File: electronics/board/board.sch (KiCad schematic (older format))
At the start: 55 parts, among them J1 Screw_Terminal_01x02, J10 Conn_01x02, J11 Conn_01x02, J12 Conn_01x02, J13 Conn_01x02, J14 Conn_01x02, J15 Conn_01x02, J16 Conn_01x02, J17 Conn_01x02, J18 Conn_01x02, J19 Conn_01x02, J2 Screw_Terminal_01x02, J20 Conn_01x02, J21 Conn_01x02, J22 Conn_01x02, J3 AVR-ISP-6, J4 USB_B_Micro, J5 Screw_Terminal_01x02, J6 Screw_Terminal_01x02, J7 Conn_01x02, J8 Conn_01x02, J9 Conn_01x02, Q1 IRF7404, SW1 SW_Push_Open_Dual, U1 LMV358, U2 ATmega32U4-AU, U3 LM7805_TO220, U4 ST485EBDR, U5 ULN2803A, U6 ULN2803A, Y1 Crystal 16MHz

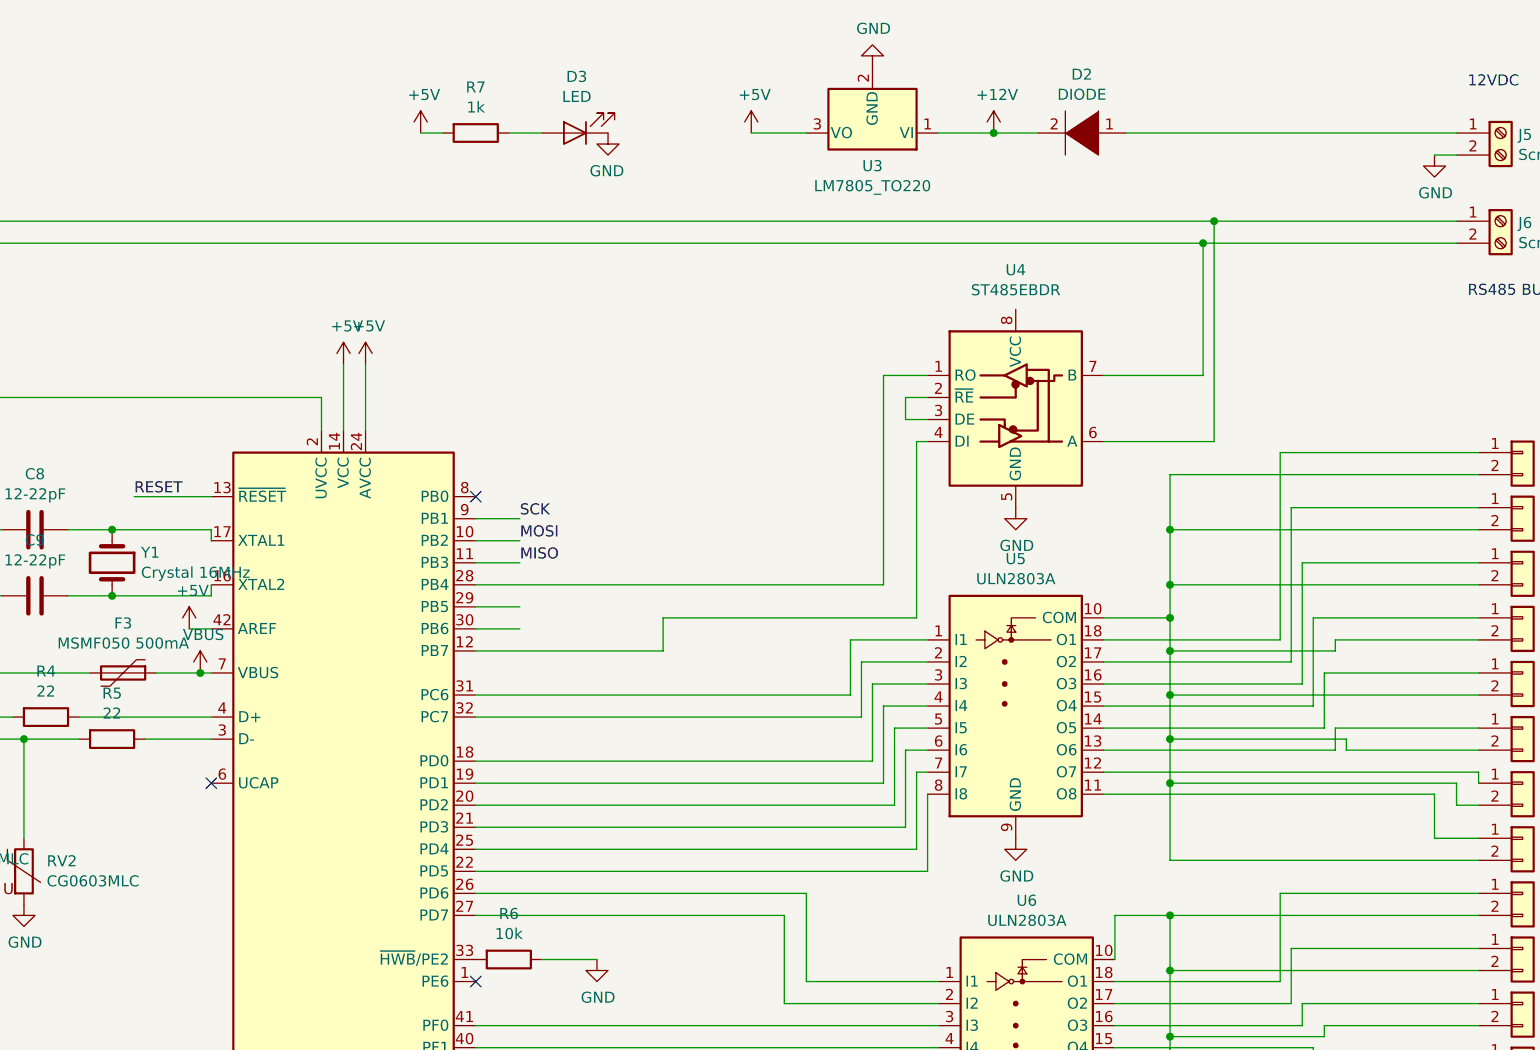
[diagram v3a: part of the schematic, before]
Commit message: 485 corrections
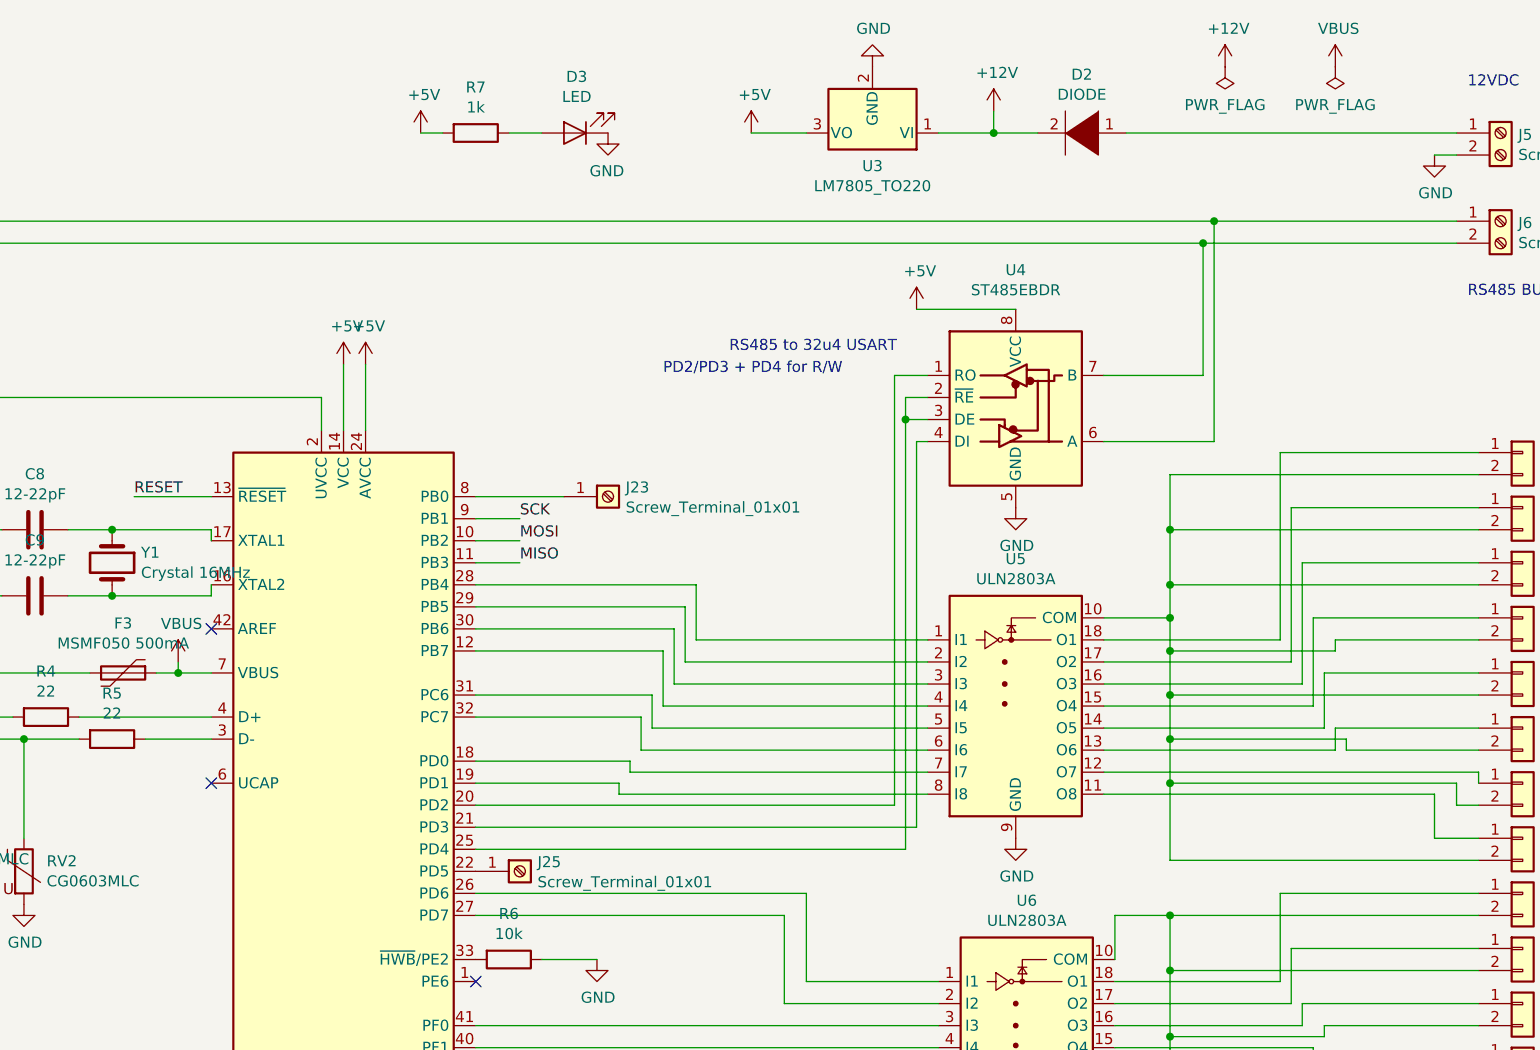
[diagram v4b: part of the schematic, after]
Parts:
- added J23, J25: Screw_Terminal_01x01, TestPoint:TestPoint_Keystone_5005-5009_Compact, symbol Connector:Screw_Terminal_01x01
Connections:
- net +5V: now also U4.8 (VCC); no longer U2.42 (AREF)
- net at U5.1 (I1): now also U2.28 (PB4); no longer U2.31 (PC6)
- net at U5.2 (I2): now also U2.29 (PB5); no longer U2.32 (PC7)
- net at U5.3 (I3): now also U2.30 (PB6); no longer U2.18 (PD0)
- net at U5.4 (I4): now also U2.12 (PB7); no longer U2.19 (PD1)
- net at U5.5 (I5): now also U2.31 (PC6); no longer U2.20 (PD2)
- net at U5.6 (I6): now also U2.32 (PC7); no longer U2.21 (PD3)
- net at U5.7 (I7): now also U2.18 (PD0); no longer U2.25 (PD4)
- net at U5.8 (I8): now also U2.19 (PD1); no longer U2.22 (PD5)
- net at U4.1 (RO): now also U2.20 (PD2); no longer U2.28 (PB4)
- net at U4.2 (~RE), U4.3 (DE): now also U2.25 (PD4)
- net at U4.4 (DI): now also U2.21 (PD3); no longer U2.12 (PB7)
- net at U2.8 (PB0): now also J23.1 (Pin_1)
- new net: J25.1 (Pin_1), U2.22 (PD5)
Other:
- note added: "PD2/PD3 + PD4 for R/W"
- note added: "RS485 to 32u4 USART"
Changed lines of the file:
@@
 Wire Wire Line
 	10650 1050 9150 1050
-Wire Wire Line
-	8750 1050 8550 1050
 $Comp
 L Device:Crystal Y1
@@
 	1    0    0    -1
 $EndComp
-Wire Wire Line
-	6200 3400 7050 3400
-Wire Wire Line
-	7050 3400 7050 3250
-Wire Wire Line
-	7050 3250 8200 3250
-Wire Wire Line
-	8200 3250 8200 2450
-Wire Wire Line
-	8200 2450 8250 2450
-Wire Wire Line
-	6200 3100 8050 3100
-Wire Wire Line
-	8050 3100 8050 2150
-Wire Wire Line
-	8050 2150 8250 2150
 $Comp
 L Amplifier_Operational:LMV358 U1
@@
 L power:+12V #PWR028
 U 1 1 5C1DBB5F
-P 8550 1050
-F 0 "#PWR028" H 8550 900 50  0001 C CNN
-F 1 "+12V" H 8565 1223 50  0000 C CNN
-F 2 "" H 8550 1050 50  0001 C CNN
-F 3 "" H 8550 1050 50  0001 C CNN
-	1    8550 1050
+P 8550 950
+F 0 "#PWR028" H 8550 800 50  0001 C CNN
+F 1 "+12V" H 8565 1123 50  0000 C CNN
+F 2 "" H 8550 950 50  0001 C CNN
+F 3 "" H 8550 950 50  0001 C CNN
+	1    8550 950
 	1    0    0    -1
 $EndComp
@@
 $EndComp
 Wire Wire Line
-	4750 3500 4950 3500
-Wire Wire Line
 	4450 3500 3750 3500
 Connection ~ 3750 3500
@@
 Wire Wire Line
 	6400 3000 6200 3000
-Connection ~ 8550 1050
-Wire Wire Line
-	8550 1050 8300 1050
 Text Label 650  4800 0    50   ~ 0
 MISO
@@
 Wire Wire Line
 	6500 4800 6750 4800
-NoConn ~ 6200 2700
 NoConn ~ 6200 4900
 Wire Wire Line
@@
 Wire Wire Line
 	5700 2100 5700 2400
-$Comp
-L power:+5V #PWR020
-U 1 1 5C1D6D5C
-P 4900 3300
-F 0 "#PWR020" H 4900 3150 50  0001 C CNN
-F 1 "+5V" H 4915 3473 50  0000 C CNN
-F 2 "" H 4900 3300 50  0001 C CNN
-F 3 "" H 4900 3300 50  0001 C CNN
-	1    4900 3300
-	1    0    0    -1
-$EndComp
-Wire Wire Line
-	4900 3300 5000 3300
 Wire Wire Line
 	8250 2350 8150 2350
@@
 Wire Wire Line
 	7700 4900 8300 4900
-Wire Wire Line
-	6200 4400 8250 4400
-Wire Wire Line
-	8250 4400 8250 4050
-Wire Wire Line
-	6200 4300 8200 4300
-Wire Wire Line
-	8200 4300 8200 3950
-Wire Wire Line
-	8200 3950 8250 3950
-Wire Wire Line
-	6200 4200 8150 4200
-Wire Wire Line
-	8150 4200 8150 3850
-Wire Wire Line
-	8150 3850 8250 3850
-Wire Wire Line
-	6200 4100 8100 4100
-Wire Wire Line
-	8100 4100 8100 3750
-Wire Wire Line
-	8100 3750 8250 3750
-Wire Wire Line
-	6200 4000 8050 4000
-Wire Wire Line
-	8050 4000 8050 3650
-Wire Wire Line
-	8050 3650 8250 3650
-Wire Wire Line
-	6200 3900 8000 3900
-Wire Wire Line
-	8000 3900 8000 3550
-Wire Wire Line
-	8000 3550 8250 3550
-Wire Wire Line
-	6200 3700 7950 3700
-Wire Wire Line
-	7950 3450 8250 3450
-Wire Wire Line
-	7950 3450 7950 3700
-Wire Wire Line
-	6200 3600 7900 3600
-Wire Wire Line
-	7900 3600 7900 3350
-Wire Wire Line
-	7900 3350 8250 3350
 $Comp
 L Switch:SW_Push_Open_Dual SW1
@@
 Wire Wire Line
 	6350 1050 6500 1050
-$Comp
-L power:VBUS #PWR037
-U 1 1 5C42ADFE
-P 4950 3500
-F 0 "#PWR037" H 4950 3350 50  0001 C CNN
-F 1 "VBUS" H 4965 3673 50  0000 C CNN
-F 2 "" H 4950 3500 50  0001 C CNN
-F 3 "" H 4950 3500 50  0001 C CNN
-	1    4950 3500
-	1    0    0    -1
-$EndComp
-Connection ~ 4950 3500
-Wire Wire Line
-	4950 3500 5000 3500
 Wire Wire Line
 	3600 3800 4150 3800
@@
 	4150 3800 4400 3800
 Wire Wire Line
-	6200 3200 6400 3200
-Wire Wire Line
-	6200 3300 6400 3300
+	8300 1050 8550 1050
+Wire Wire Line
+	8550 950  8550 1050
+Connection ~ 8550 1050
+Wire Wire Line
+	8550 1050 8750 1050
+NoConn ~ 5000 3300
+$Comp
+L power:VBUS #PWR0101
+U 1 1 5C502AD8
+P 4850 3450
+F 0 "#PWR0101" H 4850 3300 50  0001 C CNN
+F 1 "VBUS" H 4865 3623 50  0000 C CNN
+F 2 "" H 4850 3450 50  0001 C CNN
+F 3 "" H 4850 3450 50  0001 C CNN
+	1    4850 3450
+	1    0    0    -1
+$EndComp
+Wire Wire Line
+	4750 3500 4850 3500
+Wire Wire Line
+	4850 3450 4850 3500
+Connection ~ 4850 3500
+Wire Wire Line
+	4850 3500 5000 3500
+$Comp
+L power:+5V #PWR0102
+U 1 1 5C512DFB
+P 8200 1850
+F 0 "#PWR0102" H 8200 1700 50  0001 C CNN
+F 1 "+5V" H 8215 2023 50  0000 C CNN
+F 2 "" H 8200 1850 50  0001 C CNN
+F 3 "" H 8200 1850 50  0001 C CNN
+	1    8200 1850
+	1    0    0    -1
+$EndComp
+Wire Wire Line
+	8200 1850 8650 1850
+$Comp
+L Connector:Screw_Terminal_01x01 J23
+U 1 1 5C537729
+P 6800 2700
+F 0 "J23" H 6880 2742 50  0000 L CNN
+F 1 "Screw_Terminal_01x01" H 6880 2651 50  0000 L CNN
+F 2 "TestPoint:TestPoint_Keystone_5005-5009_Compact" H 6800 2700 50  0001 C CNN
+F 3 "~" H 6800 2700 50  0001 C CNN
+	1    6800 2700
+	1    0    0    -1
+$EndComp
+$Comp
+L Connector:Screw_Terminal_01x01 J25
+U 1 1 5C546B42
+P 6400 4400
+F 0 "J25" H 6480 4442 50  0000 L CNN
+F 1 "Screw_Terminal_01x01" H 6480 4351 50  0000 L CNN
+F 2 "TestPoint:TestPoint_Keystone_5005-5009_Compact" H 6400 4400 50  0001 C CNN
+F 3 "~" H 6400 4400 50  0001 C CNN
+	1    6400 4400
+	1    0    0    -1
+$EndComp
+$Comp
+L power:+12V #PWR0103
+U 1 1 5C5271C0
+P 9600 750
+F 0 "#PWR0103" H 9600 600 50  0001 C CNN
+F 1 "+12V" H 9615 923 50  0000 C CNN
+F 2 "" H 9600 750 50  0001 C CNN
+F 3 "" H 9600 750 50  0001 C CNN
+	1    9600 750
+	1    0    0    -1
+$EndComp
+$Comp
+L power:PWR_FLAG #FLG0101
+U 1 1 5C5270D2
+P 9600 750
+F 0 "#FLG0101" H 9600 825 50  0001 C CNN
+F 1 "PWR_FLAG" H 9600 923 50  0000 C CNN
+F 2 "" H 9600 750 50  0001 C CNN
+F 3 "~" H 9600 750 50  0001 C CNN
+	1    9600 750
+	-1   0    0    1
+$EndComp
+Wire Wire Line
+	6200 2700 6600 2700
+$Comp
+L power:PWR_FLAG #FLG0102
+U 1 1 5C5B860D
+P 10100 750
+F 0 "#FLG0102" H 10100 825 50  0001 C CNN
+F 1 "PWR_FLAG" H 10100 923 50  0000 C CNN
+F 2 "" H 10100 750 50  0001 C CNN
+F 3 "~" H 10100 750 50  0001 C CNN
+	1    10100 750
+	-1   0    0    1
+$EndComp
+$Comp
+L power:VBUS #PWR0104
+U 1 1 5C5C88CE
+P 10100 750
+F 0 "#PWR0104" H 10100 600 50  0001 C CNN
+F 1 "VBUS" H 10115 923 50  0000 C CNN
+F 2 "" H 10100 750 50  0001 C CNN
+F 3 "" H 10100 750 50  0001 C CNN
+	1    10100 750
+	1    0    0    -1
+$EndComp
+Wire Wire Line
+	8250 2150 8100 2150
+Wire Wire Line
+	8100 2150 8100 4100
+Wire Wire Line
+	8100 4100 6200 4100
+Text Notes 7350 2050 0    50   ~ 0
+RS485 to 32u4 USART
+Wire Wire Line
+	6200 3100 7200 3100
+Wire Wire Line
+	7200 3100 7200 3350
+Wire Wire Line
+	7200 3350 8250 3350
+Wire Wire Line
+	6200 3200 7150 3200
+Wire Wire Line
+	7150 3450 8250 3450
+Wire Wire Line
+	7150 3200 7150 3450
+Wire Wire Line
+	6200 3300 7100 3300
+Wire Wire Line
+	7100 3300 7100 3550
+Wire Wire Line
+	7100 3550 8250 3550
+Wire Wire Line
+	6200 3400 7050 3400
+Wire Wire Line
+	7050 3400 7050 3650
+Wire Wire Line
+	7050 3650 8250 3650
+Wire Wire Line
+	6200 3600 7000 3600
+Wire Wire Line
+	7000 3600 7000 3750
+Wire Wire Line
+	7000 3750 8250 3750
+Wire Wire Line
+	6200 3700 6950 3700
+Wire Wire Line
+	6950 3700 6950 3850
+Wire Wire Line
+	6950 3850 8250 3850
+Text Notes 7050 2150 0    50   ~ 0
+PD2/PD3 + PD4 for R/W
+Wire Wire Line
+	6200 3900 6900 3900
+Wire Wire Line
+	6900 3900 6900 3950
+Wire Wire Line
+	6900 3950 8250 3950
+Wire Wire Line
+	6200 4000 6850 4000
+Wire Wire Line
+	6850 4000 6850 4050
+Wire Wire Line
+	6850 4050 8250 4050
+Wire Wire Line
+	6200 4200 8200 4200
+Wire Wire Line
+	8200 4200 8200 2450
+Wire Wire Line
+	8200 2450 8250 2450
+Wire Wire Line
+	8150 2350 8150 4300
+Wire Wire Line
+	8150 4300 6200 4300
+Connection ~ 8150 2350
 $EndSCHEMATC

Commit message: Added layout
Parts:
- added R8: 1250, Resistor_SMD:R_0603_1608Metric, symbol Device:R
- SW1: footprint Button_Switch_SMD:SW_SPST_PTS645 -> Button_Switch_SMD:SW_SPST_TL3342
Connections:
- net VBUS: now also C10.1, C11.1
- net at U4.2 (~RE), U4.3 (DE): now also R8.2; no longer U2.25 (PD4)
- new net: R8.1, U2.25 (PD4)
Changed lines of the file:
@@
 F 0 "SW1" H 900 3860 50  0000 C CNN
 F 1 "SW_Push_Open_Dual" H 900 3769 50  0000 C CNN
-F 2 "Button_Switch_SMD:SW_SPST_PTS645" H 900 3850 50  0001 C CNN
+F 2 "Button_Switch_SMD:SW_SPST_TL3342" H 900 3850 50  0001 C CNN
 F 3 "" H 900 3850 50  0001 C CNN
 	1    900  3650
@@
 $EndComp
 Wire Wire Line
-	3200 6650 3600 6650
+	3200 6650 3400 6650
 $Comp
 L power:GND #PWR034
@@
 Wire Wire Line
 	8200 2450 8250 2450
-Wire Wire Line
-	8150 2350 8150 4300
-Wire Wire Line
-	8150 4300 6200 4300
-Connection ~ 8150 2350
+$Comp
+L Device:R R8
+U 1 1 5C83B16B
+P 8000 2850
+F 0 "R8" V 7793 2850 50  0000 C CNN
+F 1 "1250" V 7884 2850 50  0000 C CNN
+F 2 "Resistor_SMD:R_0603_1608Metric" V 7930 2850 50  0001 C CNN
+F 3 "~" H 8000 2850 50  0001 C CNN
+	1    8000 2850
+	-1   0    0    1
+$EndComp
+Wire Wire Line
+	8000 2700 8000 2250
+Wire Wire Line
+	8000 2250 8150 2250
+Connection ~ 8150 2250
+Wire Wire Line
+	8000 3000 8000 4300
+Wire Wire Line
+	8000 4300 6200 4300
+Wire Wire Line
+	3400 6650 3400 6600
+Connection ~ 3400 6650
+Wire Wire Line
+	3400 6650 3600 6650
 $EndSCHEMATC

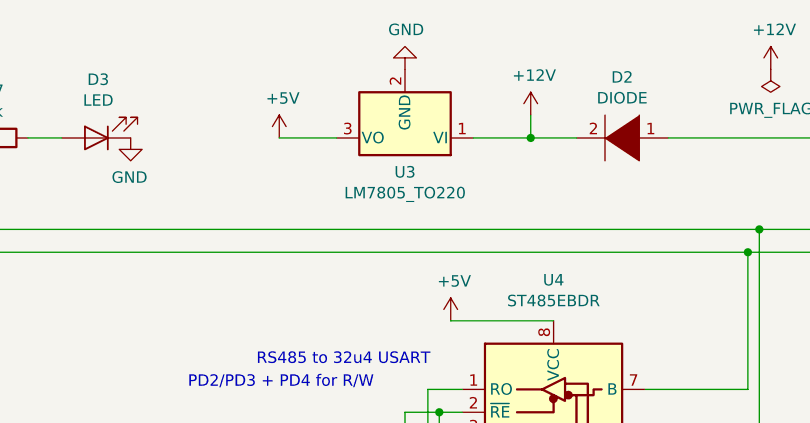
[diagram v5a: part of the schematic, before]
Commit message: 5V regulator bug
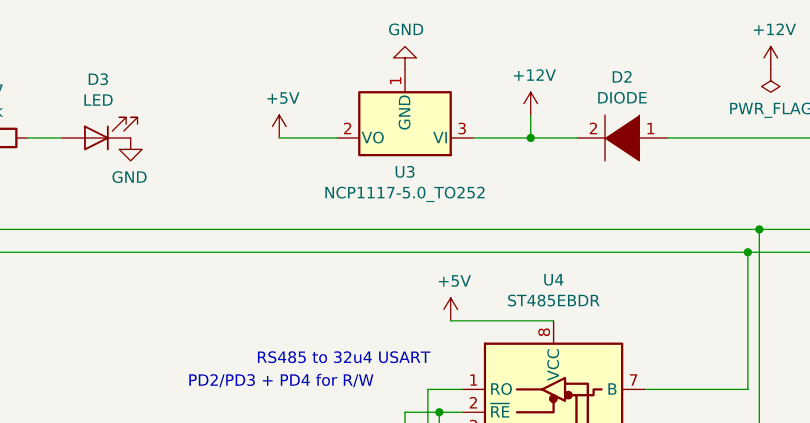
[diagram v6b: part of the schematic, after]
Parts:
- removed U3: LM7805_TO220, Package_TO_SOT_THT:TO-220-3_Vertical, symbol Regulator_Linear:LM7805_TO220
- added U3: NCP1117-5.0_TO252, Package_TO_SOT_SMD:TO-252-2, symbol Regulator_Linear:NCP1117-5.0_TO252
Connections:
- net +12V: now also U3.3 (VI)
- net +5V: now also U3.2 (VO)
- net GND: now also U3.1 (GND)
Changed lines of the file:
@@
-$EndComp
-$Comp
-L Regulator_Linear:LM7805_TO220 U3
-U 1 1 5BF587E9
-P 8000 1050
-F 0 "U3" H 8000 1200 50  0000 C CNN
-F 1 "LM7805_TO220" H 8000 1291 50  0000 C CNN
-F 2 "Package_TO_SOT_THT:TO-220-3_Vertical" H 8000 1275 50  0001 C CIN
-F 3 "http://www.fairchildsemi.com/ds/LM/LM7805.pdf" H 8000 1000 50  0001 C CNN
-	1    8000 1050
-	-1   0    0    1
 $EndComp
 $Comp
@@
 Wire Wire Line
 	3400 6650 3600 6650
+$Comp
+L Regulator_Linear:NCP1117-5.0_TO252 U3
+U 1 1 5C8808F5
+P 8000 1050
+F 0 "U3" H 8000 1200 50  0000 C CNN
+F 1 "NCP1117-5.0_TO252" H 8000 1291 50  0000 C CNN
+F 2 "Package_TO_SOT_SMD:TO-252-2" H 8000 1275 50  0001 C CNN
+F 3 "http://www.onsemi.com/pub_link/Collateral/NCP1117-D.PDF" H 8000 1050 50  0001 C CNN
+	1    8000 1050
+	-1   0    0    1
+$EndComp
 $EndSCHEMATC

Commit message: Routing update
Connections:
- net +12V: no longer J1.1 (Pin_1)
- net at D2.1 (K), J5.1 (Pin_1): now also J1.1 (Pin_1)
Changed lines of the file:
@@
 Wire Wire Line
 	650  6800 950  6800
-Wire Wire Line
-	1500 1050 1000 1050
 $Comp
 L power:+5V #PWR04
@@
 $EndComp
 $Comp
-L power:+12V #PWR07
-U 1 1 5C1E1209
-P 1500 1050
-F 0 "#PWR07" H 1500 900 50  0001 C CNN
-F 1 "+12V" H 1515 1223 50  0000 C CNN
-F 2 "" H 1500 1050 50  0001 C CNN
-F 3 "" H 1500 1050 50  0001 C CNN
-	1    1500 1050
-	1    0    0    -1
-$EndComp
-$Comp
 L power:+12V #PWR01
 U 1 1 5C1E67F9
@@
 	-1   0    0    1
 $EndComp
+Wire Wire Line
+	5250 1050 5250 1400
+Wire Wire Line
+	5250 1400 9150 1400
+Wire Wire Line
+	9150 1400 9150 1050
+Wire Wire Line
+	1000 1050 5250 1050
+Connection ~ 9150 1050
 $EndSCHEMATC

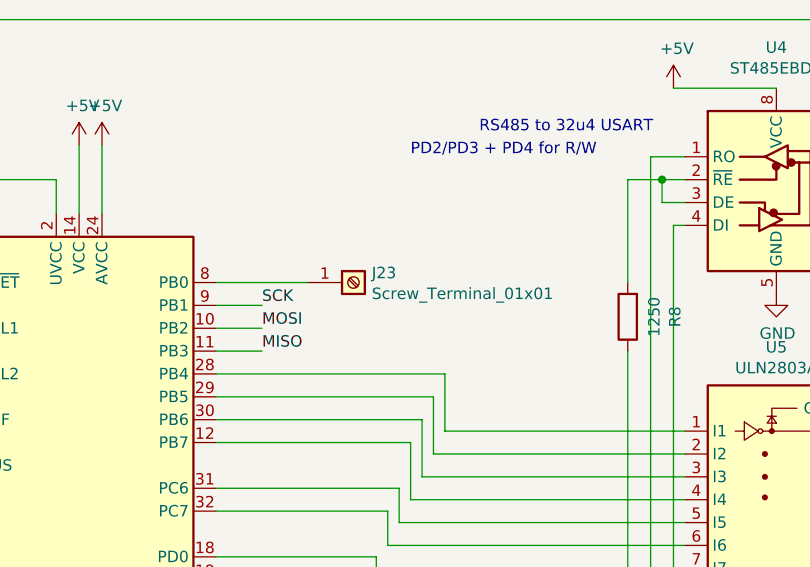
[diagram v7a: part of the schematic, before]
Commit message: GND + mounting holes
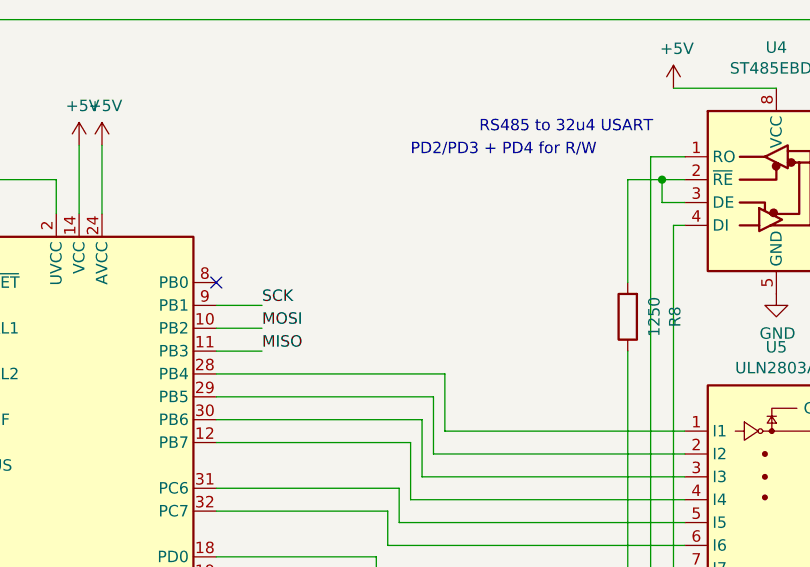
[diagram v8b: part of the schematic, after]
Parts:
- removed J23: Screw_Terminal_01x01, TestPoint:TestPoint_Keystone_5005-5009_Compact, symbol Connector:Screw_Terminal_01x01
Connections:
- no-connect marks 4 -> 5
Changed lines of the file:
@@
 	8200 1850 8650 1850
-$Comp
-L Connector:Screw_Terminal_01x01 J23
-U 1 1 5C537729
-P 6800 2700
-F 0 "J23" H 6880 2742 50  0000 L CNN
-F 1 "Screw_Terminal_01x01" H 6880 2651 50  0000 L CNN
-F 2 "TestPoint:TestPoint_Keystone_5005-5009_Compact" H 6800 2700 50  0001 C CNN
-F 3 "~" H 6800 2700 50  0001 C CNN
-	1    6800 2700
-	1    0    0    -1
-$EndComp
 $Comp
 L Connector:Screw_Terminal_01x01 J25
@@
 	-1   0    0    1
 $EndComp
-Wire Wire Line
-	6200 2700 6600 2700
 $Comp
 L power:PWR_FLAG #FLG0102
@@
 	1000 1050 5250 1050
 Connection ~ 9150 1050
+NoConn ~ 6200 2700
 $EndSCHEMATC
